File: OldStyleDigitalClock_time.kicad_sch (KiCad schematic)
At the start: 18 parts, among them U14 NA555P, U3 CD4060BE, U6 CD4017BE, U7 CD4017BE, U8 CD4017BE, Y1 HC49 XTAL (32768 Hz)

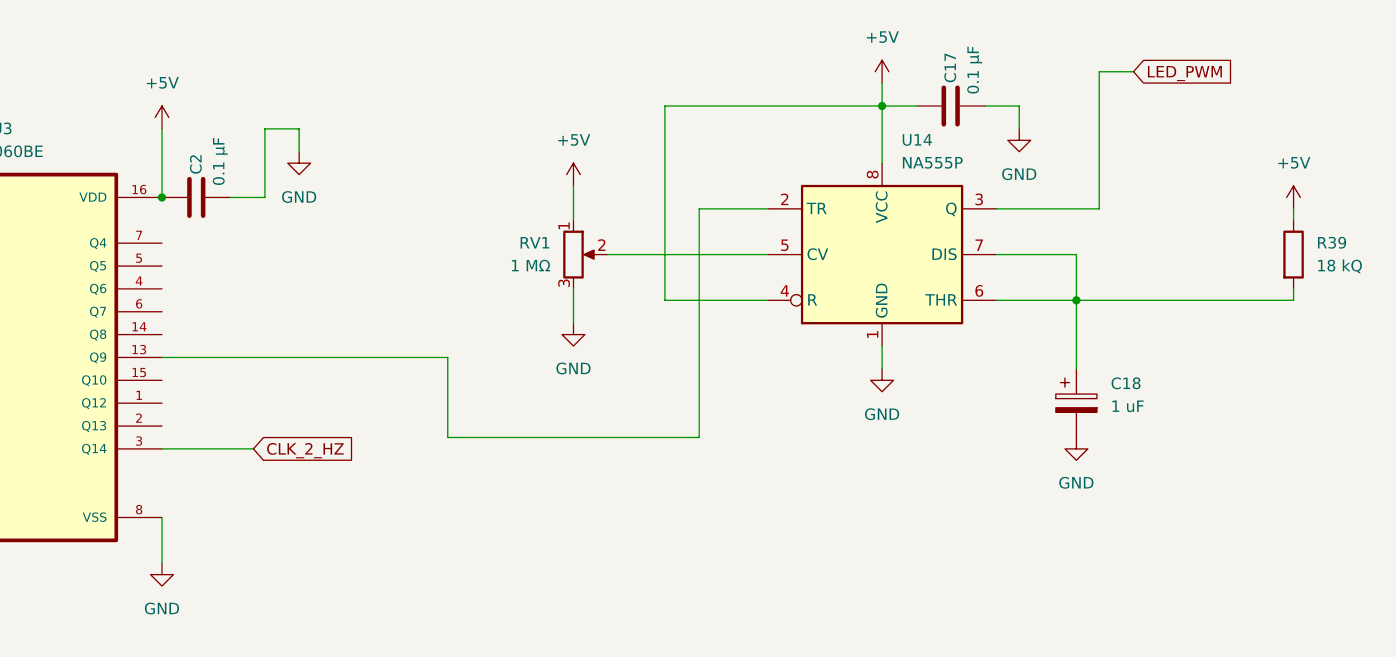
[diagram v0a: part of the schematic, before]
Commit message: Using standard astable multivibrator for LED dimming
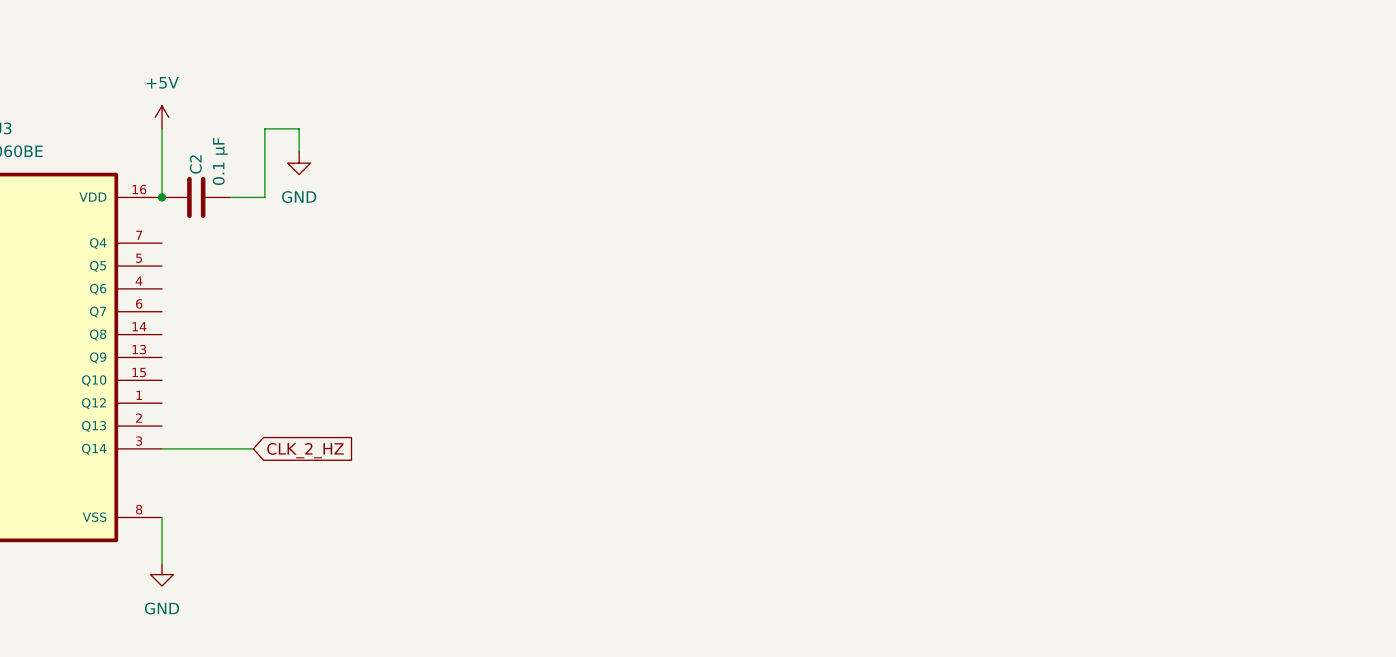
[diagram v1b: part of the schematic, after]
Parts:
- removed C17: 0.1 µF, Capacitor_THT:C_Disc_D5.1mm_W3.2mm_P5.00mm, symbol Device:C
- removed C18: 1 uF, symbol Device:C_Polarized
- removed R39: 18 kQ, symbol Device:R
- removed RV1: 1 MΩ, symbol Device:R_Potentiometer
- removed U14: NA555P, Package_DIP:DIP-8_W7.62mm, symbol Timer:NA555P
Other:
- company: (none) -> Pasquale Lafiosca
- title: (none) -> Old style digital clock

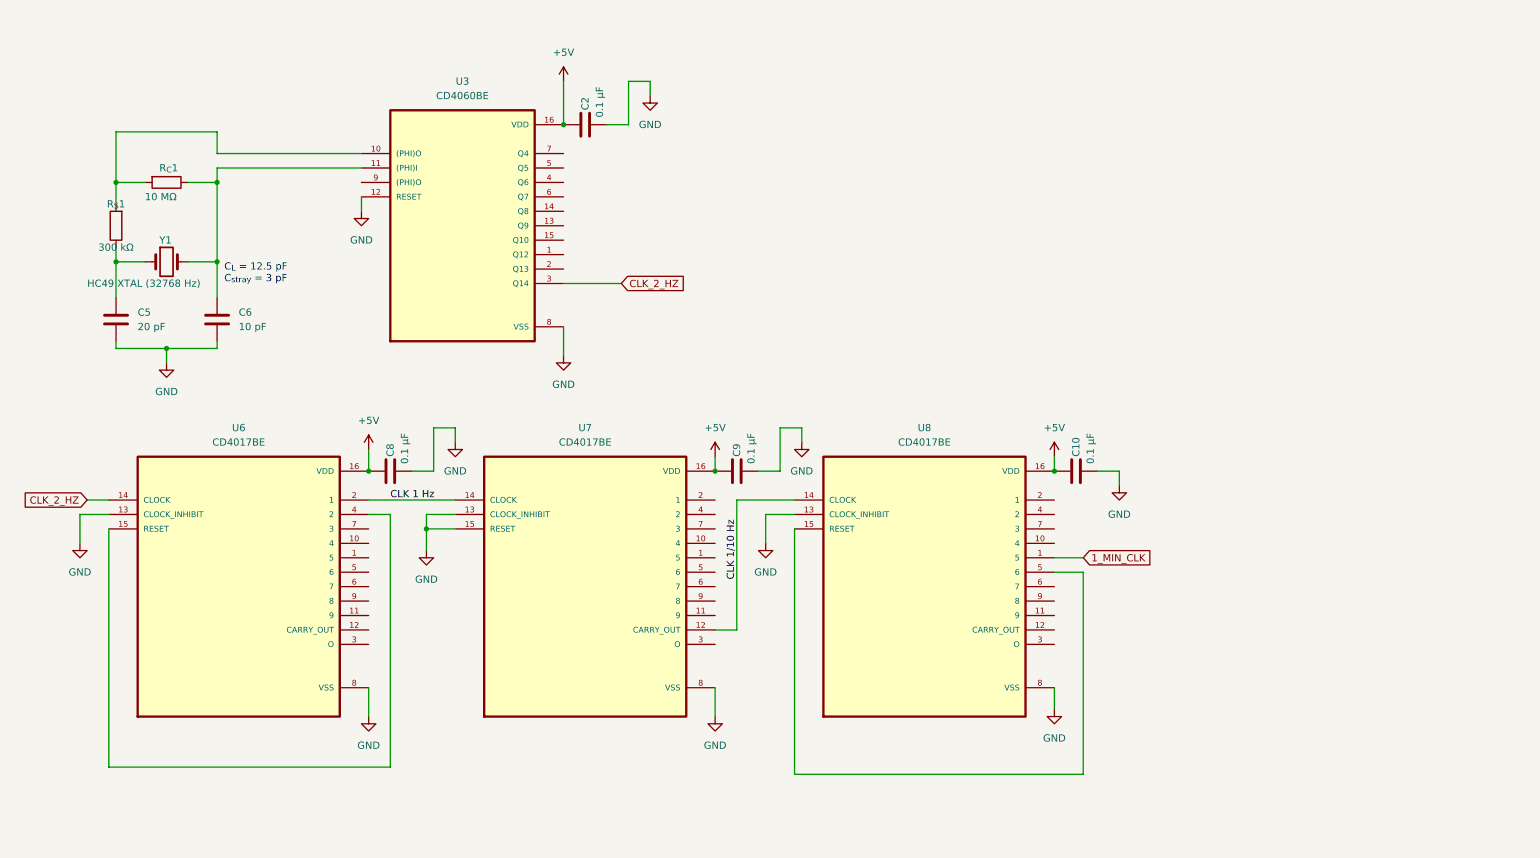
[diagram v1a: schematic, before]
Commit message: Updated PWM calculations
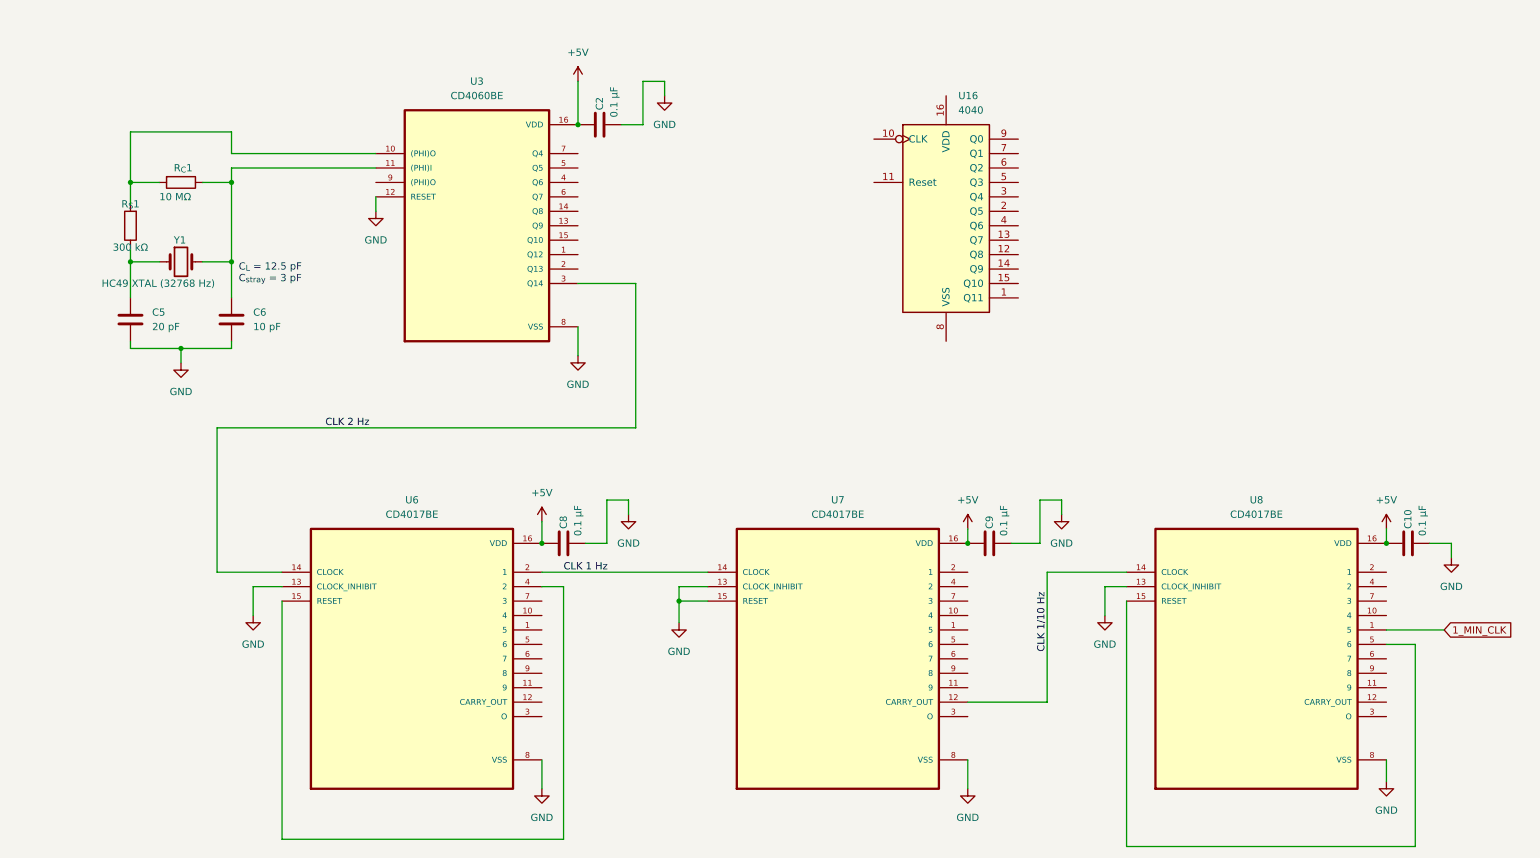
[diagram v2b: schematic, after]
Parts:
- added U16: 4040, symbol 4xxx:4040
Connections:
- net CLK_2_HZ renamed CLK 2 Hz
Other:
- moved on the sheet: C10, C2, C5, C6, C8, C9, R_{C}1, R_{S}1, U3, U6, U7, U8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

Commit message: Partial commit: Moved to SMD footprints
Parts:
- C14: renamed from C2; footprint Capacitor_THT:C_Disc_D5.1mm_W3.2mm_P5.00mm -> Capacitor_SMD:C_1206_3216Metric
- C15: renamed from C5; footprint Capacitor_THT:C_Disc_D5.1mm_W3.2mm_P5.00mm -> Capacitor_SMD:C_1206_3216Metric
- C16: renamed from C6; footprint Capacitor_THT:C_Disc_D5.1mm_W3.2mm_P5.00mm -> Capacitor_SMD:C_1206_3216Metric
- C17: renamed from C8; footprint Capacitor_THT:C_Disc_D5.1mm_W3.2mm_P5.00mm -> Capacitor_SMD:C_1206_3216Metric
- C18: renamed from C9; footprint Capacitor_THT:C_Disc_D5.1mm_W3.2mm_P5.00mm -> Capacitor_SMD:C_1206_3216Metric
- C19: renamed from C10; footprint Capacitor_THT:C_Disc_D5.1mm_W3.2mm_P5.00mm -> Capacitor_SMD:C_1206_3216Metric
- R_{C}1, R_{S}1: footprint Resistor_THT:R_Axial_DIN0204_L3.6mm_D1.6mm_P7.62mm_Horizontal -> Resistor_SMD:R_1206_3216Metric
- renumbered U16 to U12, U3 to U13, U6 to U14, U7 to U15, U8 to U16

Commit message: Removed old footprints
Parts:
- U13: footprint CD4060BE:DIP794W45P254L1969H508Q16 -> (none)
- U14, U15, U16: footprint CD4017BE:DIP794W45P254L1969H508Q16 -> (none)
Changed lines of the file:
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@@
 			)
 		)
-		(property "Footprint" "CD4017BE:DIP794W45P254L1969H508Q16"
+		(property "Footprint" ""
 			(at 83.82 125.73 0)
 			(effects
@@
 			)
 		)
-		(property "Footprint" "CD4060BE:DIP794W45P254L1969H508Q16"
+		(property "Footprint" ""
 			(at 95.25 49.53 0)
 			(effects
@@
 			)
 		)
-		(property "Footprint" "CD4017BE:DIP794W45P254L1969H508Q16"
+		(property "Footprint" ""
 			(at 158.75 125.73 0)
 			(effects
@@
 			)
 		)
-		(property "Footprint" "CD4017BE:DIP794W45P254L1969H508Q16"
+		(property "Footprint" ""
 			(at 232.41 125.73 0)
 			(effects

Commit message: Assigned footprints: first draft
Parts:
- removed U12: 4040, symbol 4xxx:4040
- U13, U14, U15, U16: footprint (none) -> Package_SO:SOIC-16W_5.3x10.2mm_P1.27mm
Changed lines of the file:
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@@
-	)
-	(symbol
-		(lib_id "4xxx:4040")
-		(at 177.8 46.99 0)
-		(unit 1)
-		(exclude_from_sim no)
-		(in_bom yes)
-		(on_board yes)
-		(dnp no)
-		(fields_autoplaced yes)
-		(property "Reference" "U12"
-			(at 179.9433 26.67 0)
-			(effects
-				(font
-					(size 1.27 1.27)
-				)
-				(justify left)
-			)
-		)
-		(property "Value" "4040"
-			(at 179.9433 29.21 0)
-			(effects
-				(font
-					(size 1.27 1.27)
-				)
-				(justify left)
-			)
-		)
-		(property "Footprint" ""
-			(at 177.8 46.99 0)
-			(effects
-				(font
-					(size 1.27 1.27)
-				)
-				(hide yes)
-			)
-		)
-		(property "Datasheet" "http://www.intersil.com/content/dam/Intersil/documents/cd40/cd4020bms-24bms-40bms.pdf"
-			(at 177.8 46.99 0)
-			(effects
-				(font
-					(size 1.27 1.27)
-				)
-				(hide yes)
-			)
-		)
-		(property "Description" "Binary Counter 12 stages (Asynchronous)"
-			(at 177.8 46.99 0)
-			(effects
-				(font
-					(size 1.27 1.27)
-				)
-				(hide yes)
-			)
-		)
-		(pin "2"
-		)
-		(pin "14"
-		)
-		(pin "15"
-		)
-		(pin "5"
-		)
-		(pin "4"
-		)
-		(pin "16"
-		)
-		(pin "13"
-		)
-		(pin "1"
-		)
-		(pin "10"
-		)
-		(pin "7"
-		)
-		(pin "6"
-		)
-		(pin "9"
-		)
-		(pin "11"
-		)
-		(pin "12"
-		)
-		(pin "3"
-		)
-		(pin "8"
-		)
-		(instances
-			(project ""
-				(path "/a24f1d5b-eb61-47a3-9a92-6515e74f7a21/1c160f5e-c878-4380-a841-1716d7aeea05"
-					(reference "U12")
-					(unit 1)
-				)
-			)
-		)
 	)
 	(symbol
@@
 			)
 		)
-		(property "Footprint" ""
+		(property "Footprint" "Package_SO:SOIC-16W_5.3x10.2mm_P1.27mm"
 			(at 83.82 125.73 0)
 			(effects
@@
 			)
 		)
-		(property "Footprint" ""
+		(property "Footprint" "Package_SO:SOIC-16W_5.3x10.2mm_P1.27mm"
 			(at 95.25 49.53 0)
 			(effects
@@
 			)
 		)
-		(property "Footprint" ""
+		(property "Footprint" "Package_SO:SOIC-16W_5.3x10.2mm_P1.27mm"
 			(at 158.75 125.73 0)
 			(effects
@@
 			)
 		)
-		(property "Footprint" ""
+		(property "Footprint" "Package_SO:SOIC-16W_5.3x10.2mm_P1.27mm"
 			(at 232.41 125.73 0)
 			(effects

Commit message: pcb rough organisation
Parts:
- renumbered U13 to U12, U14 to U13, U15 to U14, U16 to U15

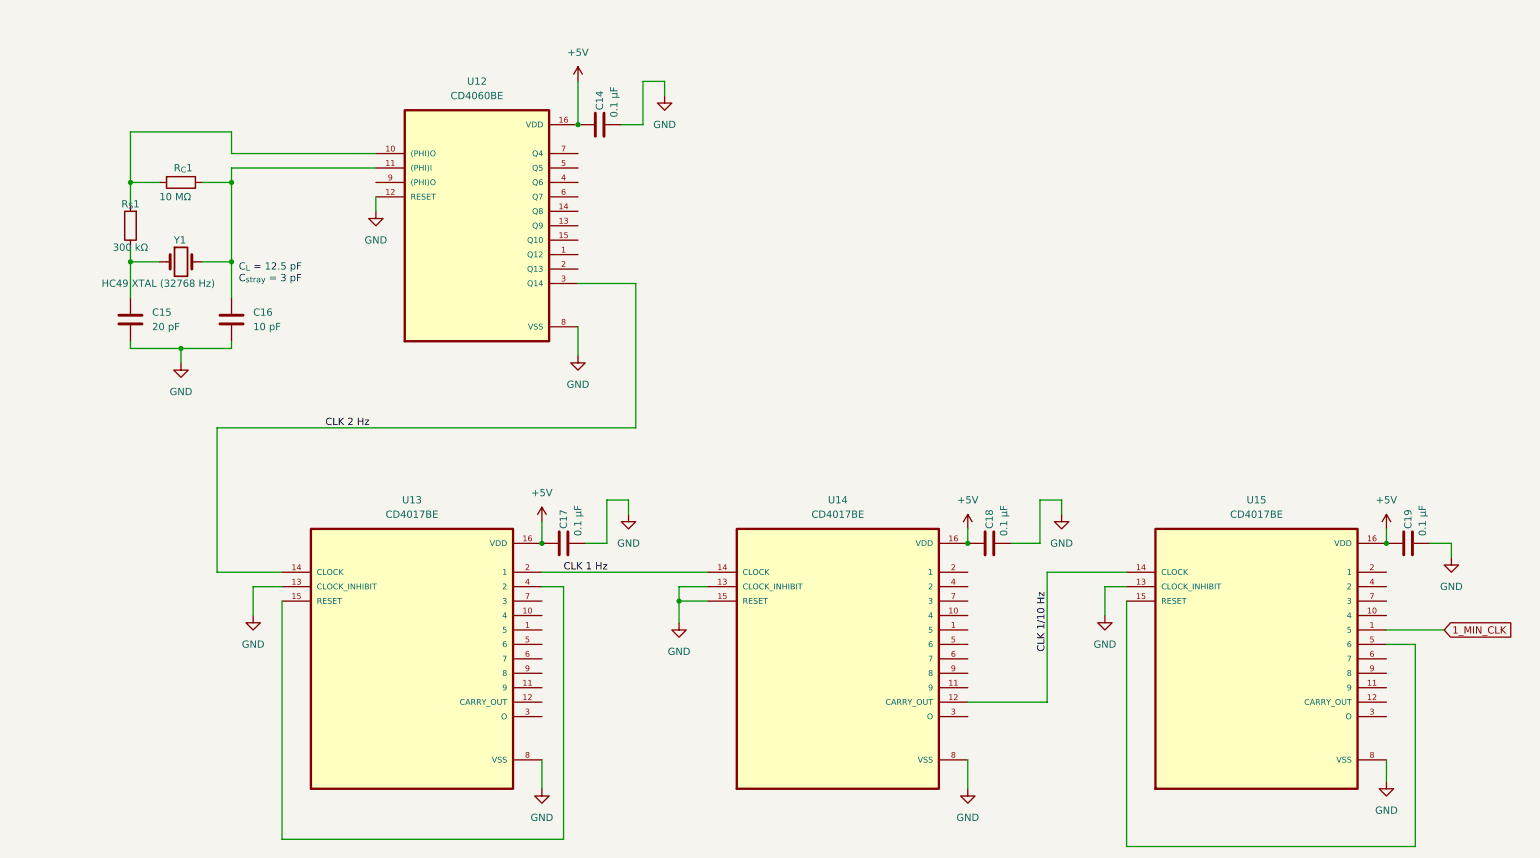
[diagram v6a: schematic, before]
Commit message: Moved USB receptacles, minor changes. Marked no connect pins.
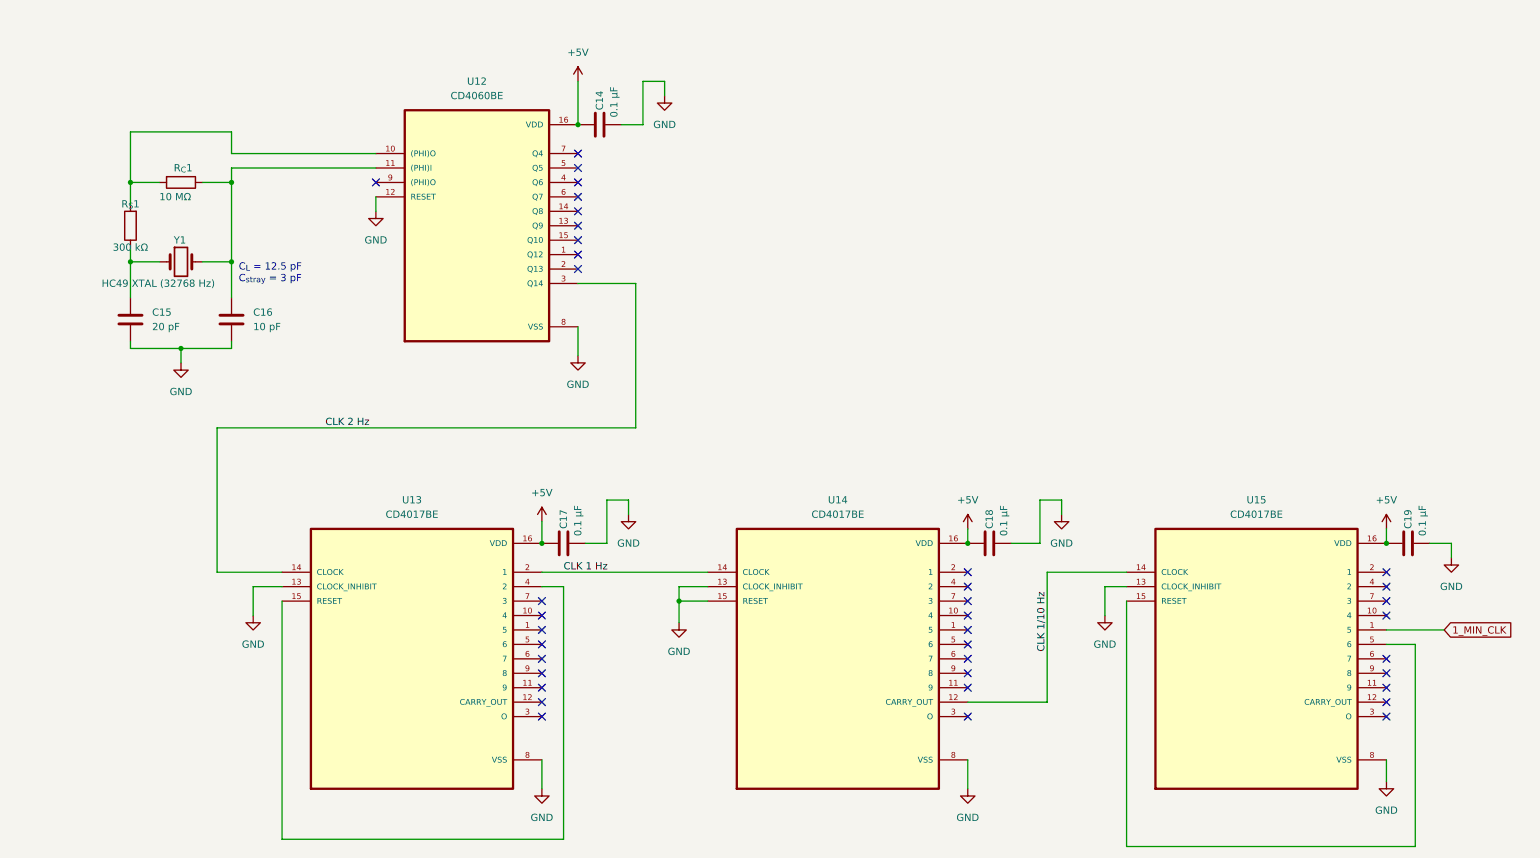
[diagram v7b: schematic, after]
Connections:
- no-connect marks 0 -> 38
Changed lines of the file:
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@@
 	(title_block
 		(title "Old style digital clock")
-		(date "2025-10-17")
+		(date "2025-11-08")
 		(rev "1")
 		(company "Pasquale Lafiosca")
@@
 		(diameter 0)
 		(color 0 0 0 0)
+	)
+	(no_connect
+		(at 106.68 118.11)
+	)
+	(no_connect
+		(at 113.03 46.99)
+	)
+	(no_connect
+		(at 113.03 49.53)
+	)
+	(no_connect
+		(at 255.27 130.81)
+	)
+	(no_connect
+		(at 106.68 120.65)
+	)
+	(no_connect
+		(at 106.68 135.89)
+	)
+	(no_connect
+		(at 106.68 125.73)
+	)
+	(no_connect
+		(at 255.27 110.49)
+	)
+	(no_connect
+		(at 181.61 110.49)
+	)
+	(no_connect
+		(at 106.68 133.35)
+	)
+	(no_connect
+		(at 113.03 57.15)
+	)
+	(no_connect
+		(at 113.03 36.83)
+	)
+	(no_connect
+		(at 113.03 39.37)
+	)
+	(no_connect
+		(at 181.61 118.11)
+	)
+	(no_connect
+		(at 255.27 128.27)
+	)
+	(no_connect
+		(at 106.68 128.27)
+	)
+	(no_connect
+		(at 181.61 125.73)
+	)
+	(no_connect
+		(at 181.61 123.19)
+	)
+	(no_connect
+		(at 106.68 123.19)
+	)
+	(no_connect
+		(at 181.61 128.27)
+	)
+	(no_connect
+		(at 255.27 113.03)
+	)
+	(no_connect
+		(at 255.27 115.57)
+	)
+	(no_connect
+		(at 113.03 52.07)
+	)
+	(no_connect
+		(at 77.47 41.91)
+	)
+	(no_connect
+		(at 106.68 130.81)
+	)
+	(no_connect
+		(at 113.03 54.61)
+	)
+	(no_connect
+		(at 113.03 44.45)
+	)
+	(no_connect
+		(at 181.61 120.65)
+	)
+	(no_connect
+		(at 181.61 113.03)
+	)
+	(no_connect
+		(at 181.61 135.89)
+	)
+	(no_connect
+		(at 181.61 115.57)
+	)
+	(no_connect
+		(at 113.03 41.91)
+	)
+	(no_connect
+		(at 181.61 130.81)
+	)
+	(no_connect
+		(at 255.27 133.35)
+	)
+	(no_connect
+		(at 255.27 125.73)
+	)
+	(no_connect
+		(at 106.68 115.57)
+	)
+	(no_connect
+		(at 255.27 135.89)
+	)
+	(no_connect
+		(at 255.27 118.11)
 	)
 	(wire
@@
 			)
 		)
-		(property "Description" "\n                        \n                            CMOS 14-Stage Ripple-Carry Binary Counter/Divider and Oscillator\n                        \n"
+		(property "Description" "CMOS 14-Stage Ripple-Carry Binary Counter/Divider and Oscillator"
 			(at 95.25 49.53 0)
 			(effects
